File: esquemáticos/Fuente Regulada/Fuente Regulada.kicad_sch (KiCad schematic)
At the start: 9 parts, among them Q1 IRLZ24

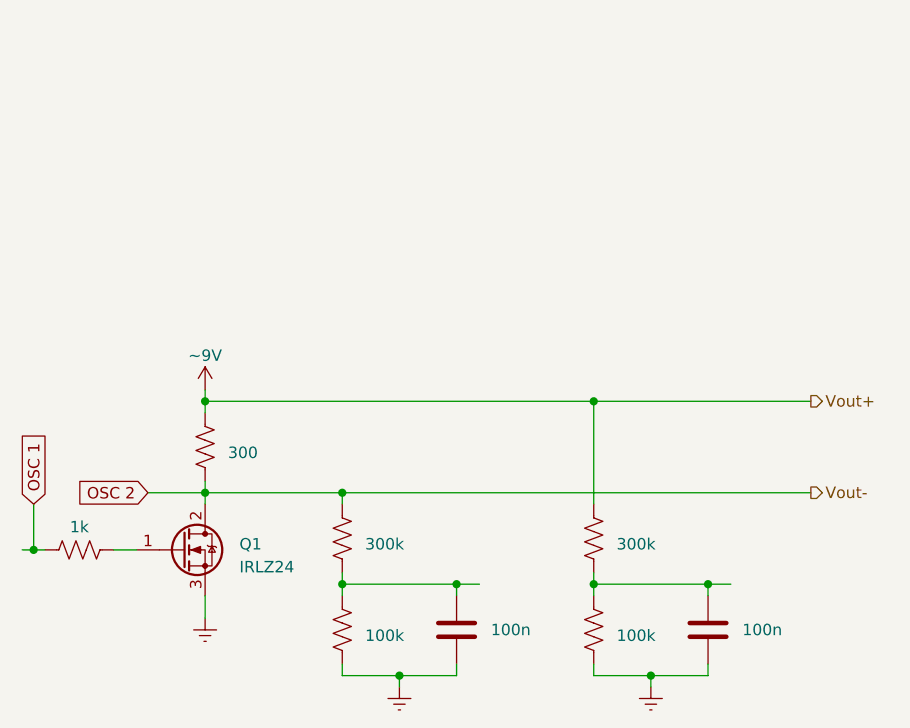
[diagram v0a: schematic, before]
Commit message: Puente H actualizado
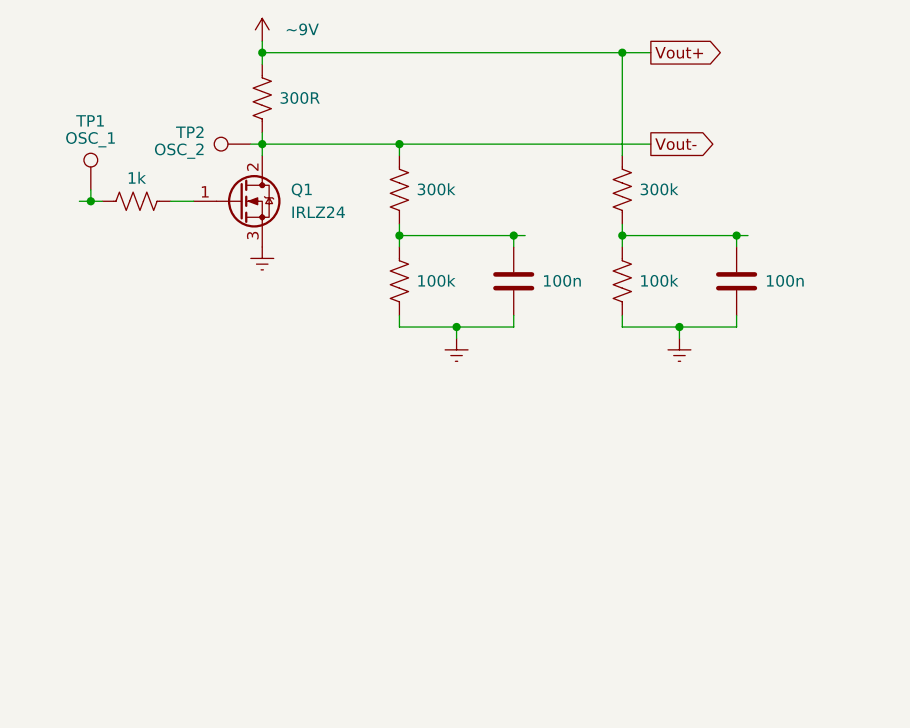
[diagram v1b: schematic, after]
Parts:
- added TP1: OSC_1, symbol Connector:TestPoint
- added TP2: OSC_2, symbol Connector:TestPoint
- R1: value 300 -> 300R
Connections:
- net OSC 1: no longer names the net of R2.1
- net OSC 1: now also TP1.1
- net OSC 2 renamed Vout-
- net Vout-: now also TP2.1
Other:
- company: (none) -> Grupo 33 - Sistemas Electrónicos Digitales
- title: (none) -> Fuente Regulada
- moved on the sheet: Q1

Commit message: Esquemáticos completos
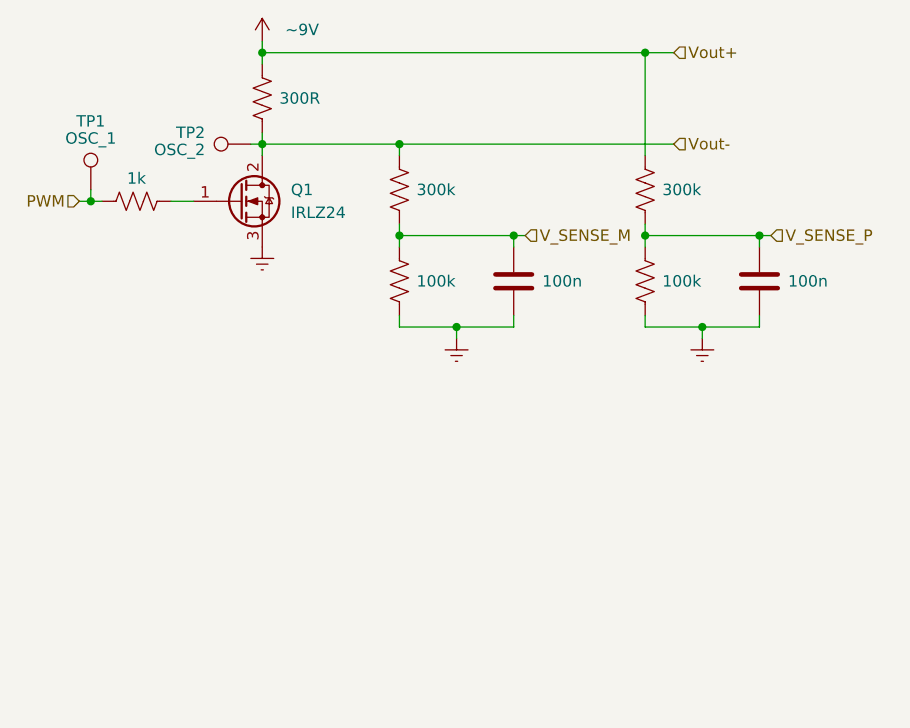
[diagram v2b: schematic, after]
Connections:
- net PWM: now reaches R2.1, TP1.1
- net V_SENSE_M: now reaches C1.1, R3.2, R4.1
- net V_SENSE_P: now reaches C2.1, R5.2, R6.1
